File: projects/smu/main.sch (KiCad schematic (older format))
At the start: 4 parts, among them P101 CONN_01X15, P102 CONN_01X28, P103 CONN_01X15, P105 CONN_01X04

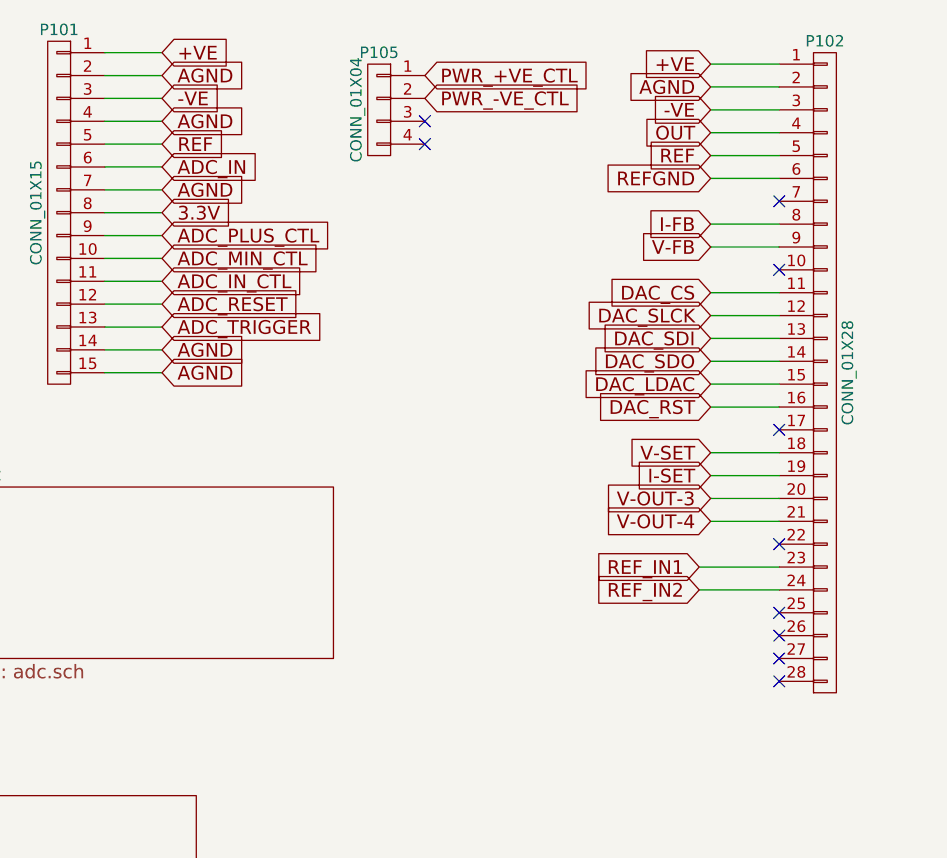
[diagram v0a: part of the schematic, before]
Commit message: add output section
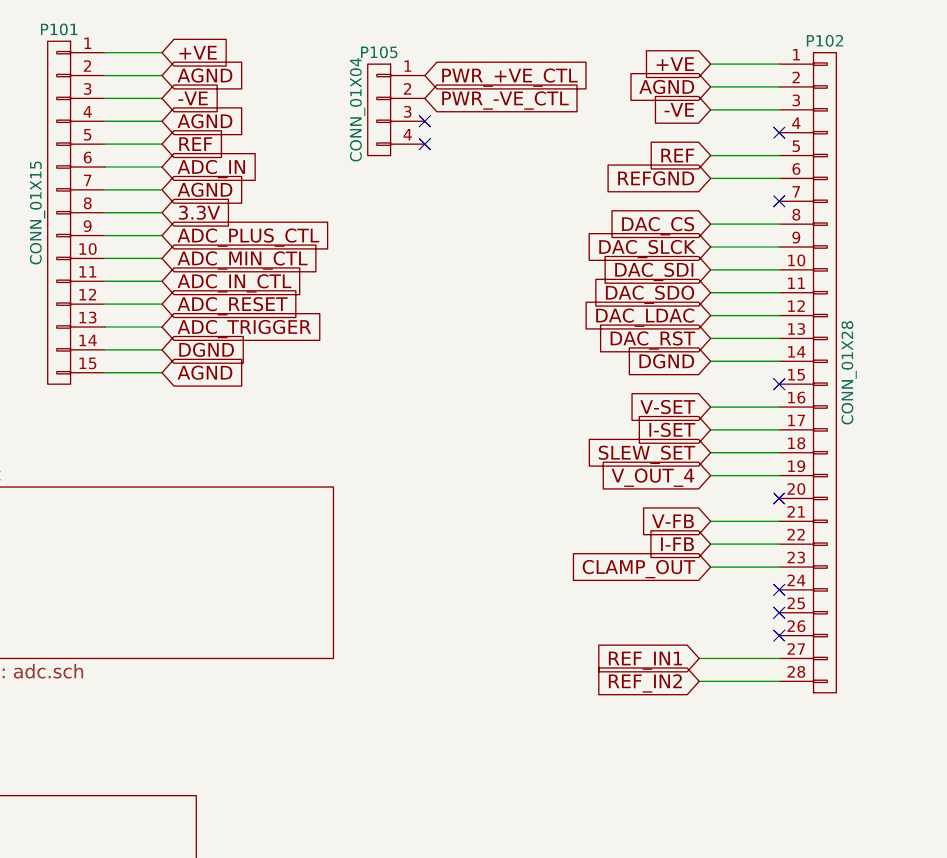
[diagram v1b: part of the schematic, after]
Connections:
- net V-OUT-4 is gone; now on net V-FB: P102.21 (P21)
- net AGND: now also P102.14 (P14)
- net DAC_CS: now also P102.8 (P8); no longer P102.11 (P11)
- net DAC_LDAC: now also P102.12 (P12); no longer P102.15 (P15)
- net DAC_RST: now also P102.13 (P13); no longer P102.16 (P16)
- net DAC_SDI: now also P102.10 (P10); no longer P102.13 (P13)
- net DAC_SDO: now also P102.11 (P11); no longer P102.14 (P14)
- net DAC_SLCK: now also P102.9 (P9); no longer P102.12 (P12)
- net I-FB: now also P102.22 (P22); no longer P102.8 (P8)
- net I-SET: now also P102.17 (P17); no longer P102.19 (P19)
- net REF_IN1: now also P102.27 (P27); no longer P102.23 (P23)
- net REF_IN2: now also P102.28 (P28); no longer P102.24 (P24)
- net V-FB: no longer P102.9 (P9)
- net V-SET: now also P102.16 (P16); no longer P102.18 (P18)
- net OUT: no longer names the net of P102.4 (P4)
- net V-OUT-3: no longer names the net of P102.20 (P20)
- new net CLAMP_OUT: P102.23 (P23)
- new net SLEW_SET: P102.18 (P18)
- new net V_OUT_4: P102.19 (P19)
- no-connect marks 22 -> 21
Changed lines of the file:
@@
 AGND
 Text GLabel 2400 2250 2    60   Input ~ 0
-AGND
+DGND
 Text GLabel 2400 2350 2    60   Input ~ 0
 AGND
 Text GLabel 2400 2150 2    60   Input ~ 0
 ADC_TRIGGER
-Wire Wire Line
-	2150 950  2400 950
-Wire Wire Line
-	2150 1050 2400 1050
-Wire Wire Line
-	2150 1150 2400 1150
-Wire Wire Line
-	2150 1350 2400 1350
-Wire Wire Line
-	2150 1450 2400 1450
-Wire Wire Line
-	2150 1650 2400 1650
-Wire Wire Line
-	2150 1750 2400 1750
-Wire Wire Line
-	2150 1850 2400 1850
-Wire Wire Line
-	2150 1250 2400 1250
-Wire Wire Line
-	2150 1550 2400 1550
-Wire Wire Line
-	2150 1950 2400 1950
-Wire Wire Line
-	2150 2050 2400 2050
-Wire Wire Line
-	2150 2150 2400 2150
-Wire Wire Line
-	2150 2250 2400 2250
-Wire Wire Line
-	2400 2350 2150 2350
-Wire Wire Line
-	5100 1000 4800 1000
-Wire Wire Line
-	5100 1100 4800 1100
-Wire Wire Line
-	5100 1200 4800 1200
-Wire Wire Line
-	5100 1300 4800 1300
-Wire Wire Line
-	4800 1400 5100 1400
-Wire Wire Line
-	5100 1800 4800 1800
-Wire Wire Line
-	4800 1700 5100 1700
 Text GLabel 7050 1500 3    60   Input ~ 0
 +VE
@@
 	1    0    0    -1
 $EndComp
-Wire Wire Line
-	7050 1300 7050 1500
 $Comp
 L PWR_FLAG #FLG02
@@
 Text GLabel 7650 1500 3    60   Input ~ 0
 -VE
-Wire Wire Line
-	7650 1300 7650 1500
-Wire Wire Line
-	4800 2000 5100 2000
-Wire Wire Line
-	4800 2100 5100 2100
-Wire Wire Line
-	4800 2200 5100 2200
-Wire Wire Line
-	4800 2300 5100 2300
-Wire Wire Line
-	4800 2400 5100 2400
-Wire Wire Line
-	4800 2500 5100 2500
 Text GLabel 9200 1400 0    60   Input ~ 0
 AGND
@@
 Text GLabel 9200 1600 0    60   Input ~ 0
 REFGND
-Wire Wire Line
-	9200 1400 9200 1600
-Wire Wire Line
-	4800 2700 5100 2700
-Wire Wire Line
-	4800 2800 5100 2800
-Wire Wire Line
-	4800 2900 5100 2900
-Wire Wire Line
-	4800 3000 5100 3000
-Wire Wire Line
-	4750 3200 5100 3200
-Wire Wire Line
-	4750 3300 5100 3300
-Wire Wire Line
-	4800 1500 5100 1500
 Text GLabel 4800 1000 0    60   Input ~ 0
 +VE
@@
 Text GLabel 4800 1400 0    60   Input ~ 0
 REF
+Text GLabel 4800 3100 0    60   Input ~ 0
+I-FB
+Text GLabel 4800 3200 0    60   Input ~ 0
+CLAMP_OUT
+Text GLabel 4800 3000 0    60   Input ~ 0
+V-FB
+Text GLabel 4800 2700 0    60   Input ~ 0
+SLEW_SET
+Text GLabel 4800 2800 0    60   Input ~ 0
+V_OUT_4
 Text GLabel 4800 1700 0    60   Input ~ 0
-I-FB
-Text GLabel 4800 1300 0    60   Input ~ 0
-OUT
-NoConn ~ 5100 1900
+DAC_CS
 Text GLabel 4800 1800 0    60   Input ~ 0
-V-FB
-Text GLabel 4800 2900 0    60   Input ~ 0
-V-OUT-3
-Text GLabel 4800 3000 0    60   Input ~ 0
-V-OUT-4
+DAC_SLCK
+Text GLabel 4800 1900 0    60   Input ~ 0
+DAC_SDI
 Text GLabel 4800 2000 0    60   Input ~ 0
-DAC_CS
+DAC_SDO
 Text GLabel 4800 2100 0    60   Input ~ 0
-DAC_SLCK
+DAC_LDAC
 Text GLabel 4800 2200 0    60   Input ~ 0
-DAC_SDI
-Text GLabel 4800 2300 0    60   Input ~ 0
-DAC_SDO
-Text GLabel 4800 2400 0    60   Input ~ 0
-DAC_LDAC
-Text GLabel 4800 2500 0    60   Input ~ 0
 DAC_RST
 Text GLabel 9200 1400 0    60   Input ~ 0
@@
 Text GLabel 9200 1600 0    60   Input ~ 0
 REFGND
-Text GLabel 4800 2700 0    60   Input ~ 0
+Text GLabel 4800 2500 0    60   Input ~ 0
 V-SET
-Text GLabel 4800 2800 0    60   Input ~ 0
+Text GLabel 4800 2600 0    60   Input ~ 0
 I-SET
 NoConn ~ 5100 1600
-NoConn ~ 5100 2600
-NoConn ~ 5100 3100
-NoConn ~ 5100 3600
-NoConn ~ 5100 3700
 Text GLabel 4800 1500 0    60   Input ~ 0
 REFGND
@@
 	1    0    0    -1
 $EndComp
-Text GLabel 4750 3300 0    60   Input ~ 0
+Text GLabel 4750 3700 0    60   Input ~ 0
 REF_IN2
-Text GLabel 4750 3200 0    60   Input ~ 0
+Text GLabel 4750 3600 0    60   Input ~ 0
 REF_IN1
 NoConn ~ 5100 3400
@@
 F1 "filter.sch" 60
 $EndSheet
+Wire Wire Line
+	2150 950  2400 950
+Wire Wire Line
+	2150 1050 2400 1050
+Wire Wire Line
+	2150 1150 2400 1150
+Wire Wire Line
+	2150 1350 2400 1350
+Wire Wire Line
+	2150 1450 2400 1450
+Wire Wire Line
+	2150 1650 2400 1650
+Wire Wire Line
+	2150 1750 2400 1750
+Wire Wire Line
+	2150 1850 2400 1850
+Wire Wire Line
+	2150 1250 2400 1250
+Wire Wire Line
+	2150 1550 2400 1550
+Wire Wire Line
+	2150 1950 2400 1950
+Wire Wire Line
+	2150 2050 2400 2050
+Wire Wire Line
+	2150 2150 2400 2150
+Wire Wire Line
+	2150 2250 2400 2250
+Wire Wire Line
+	2400 2350 2150 2350
+Wire Wire Line
+	5100 1000 4800 1000
+Wire Wire Line
+	5100 1100 4800 1100
+Wire Wire Line
+	5100 1200 4800 1200
+Wire Wire Line
+	4800 1400 5100 1400
+Wire Wire Line
+	7050 1300 7050 1500
+Wire Wire Line
+	7650 1300 7650 1500
+Wire Wire Line
+	9200 1400 9200 1600
+Wire Wire Line
+	4800 1500 5100 1500
+Wire Wire Line
+	4800 1700 5100 1700
+Wire Wire Line
+	4800 1800 5100 1800
+Wire Wire Line
+	4800 1900 5100 1900
+Wire Wire Line
+	4800 2000 5100 2000
+Wire Wire Line
+	4800 2100 5100 2100
+Wire Wire Line
+	4800 2200 5100 2200
+Text GLabel 4800 2300 0    60   Input ~ 0
+DGND
+Wire Wire Line
+	4800 2300 5100 2300
+Wire Wire Line
+	4800 2500 5100 2500
+Wire Wire Line
+	4800 2600 5100 2600
+Wire Wire Line
+	4800 2700 5100 2700
+Wire Wire Line
+	4800 2800 5100 2800
+NoConn ~ 5100 2400
+NoConn ~ 5100 2900
+Wire Wire Line
+	4800 3000 5100 3000
+Wire Wire Line
+	4800 3100 5100 3100
+Wire Wire Line
+	4800 3200 5100 3200
+NoConn ~ 5100 3300
+Wire Wire Line
+	4750 3600 5100 3600
+Wire Wire Line
+	4750 3700 5100 3700
+NoConn ~ 5100 1300
 $EndSCHEMATC

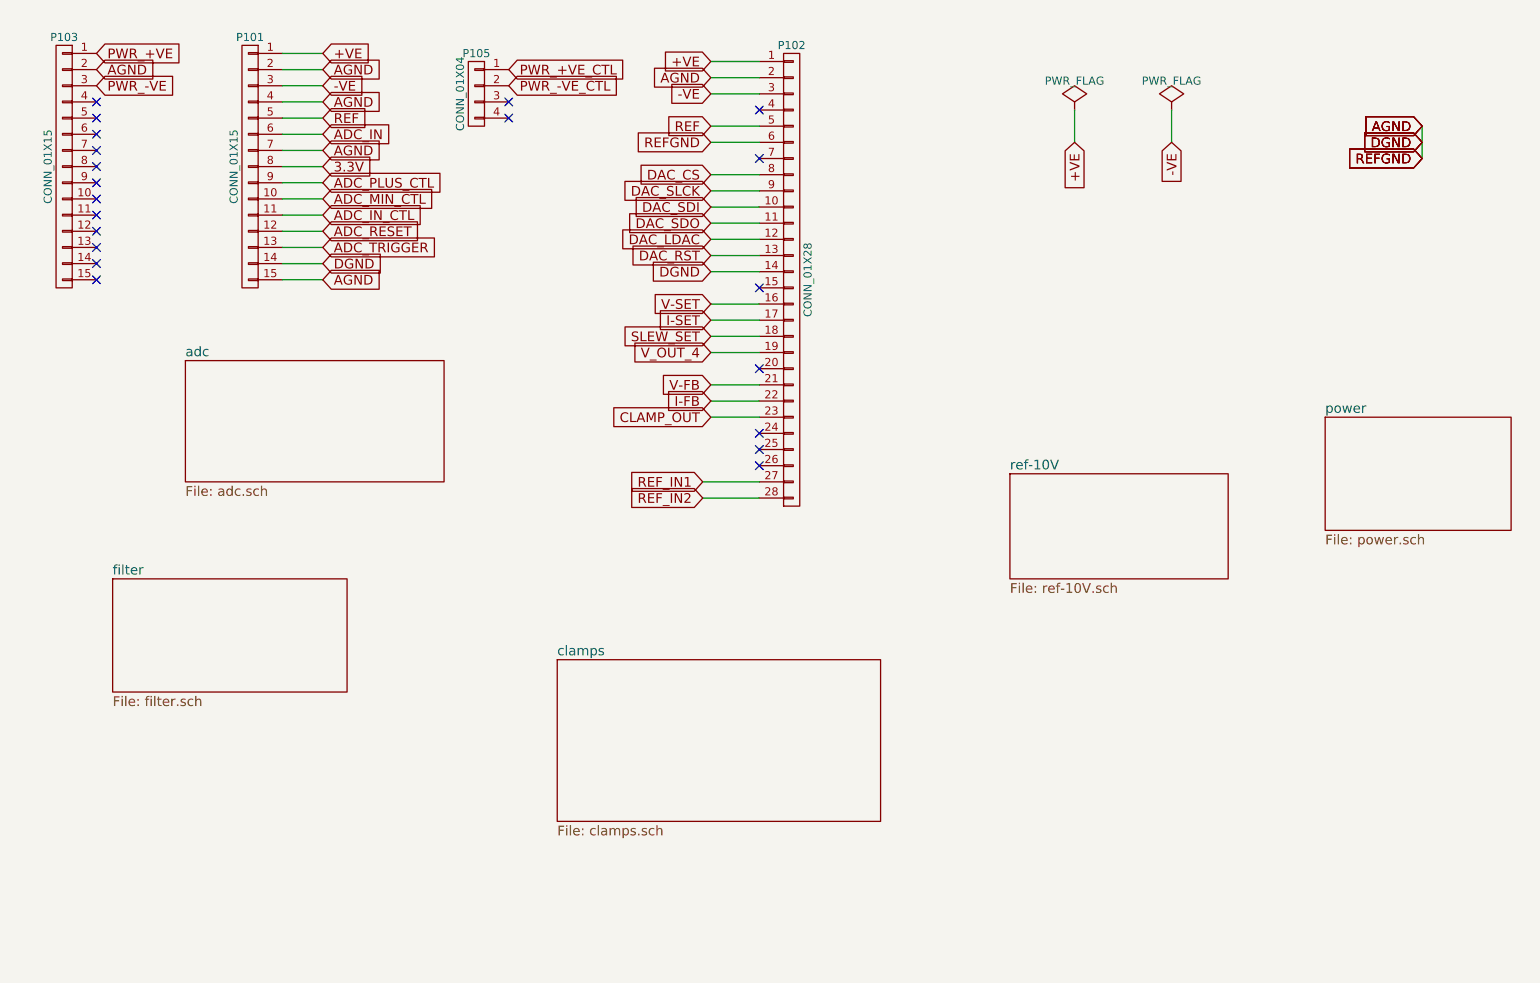
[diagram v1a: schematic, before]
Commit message: split pin-headers into analog and digital
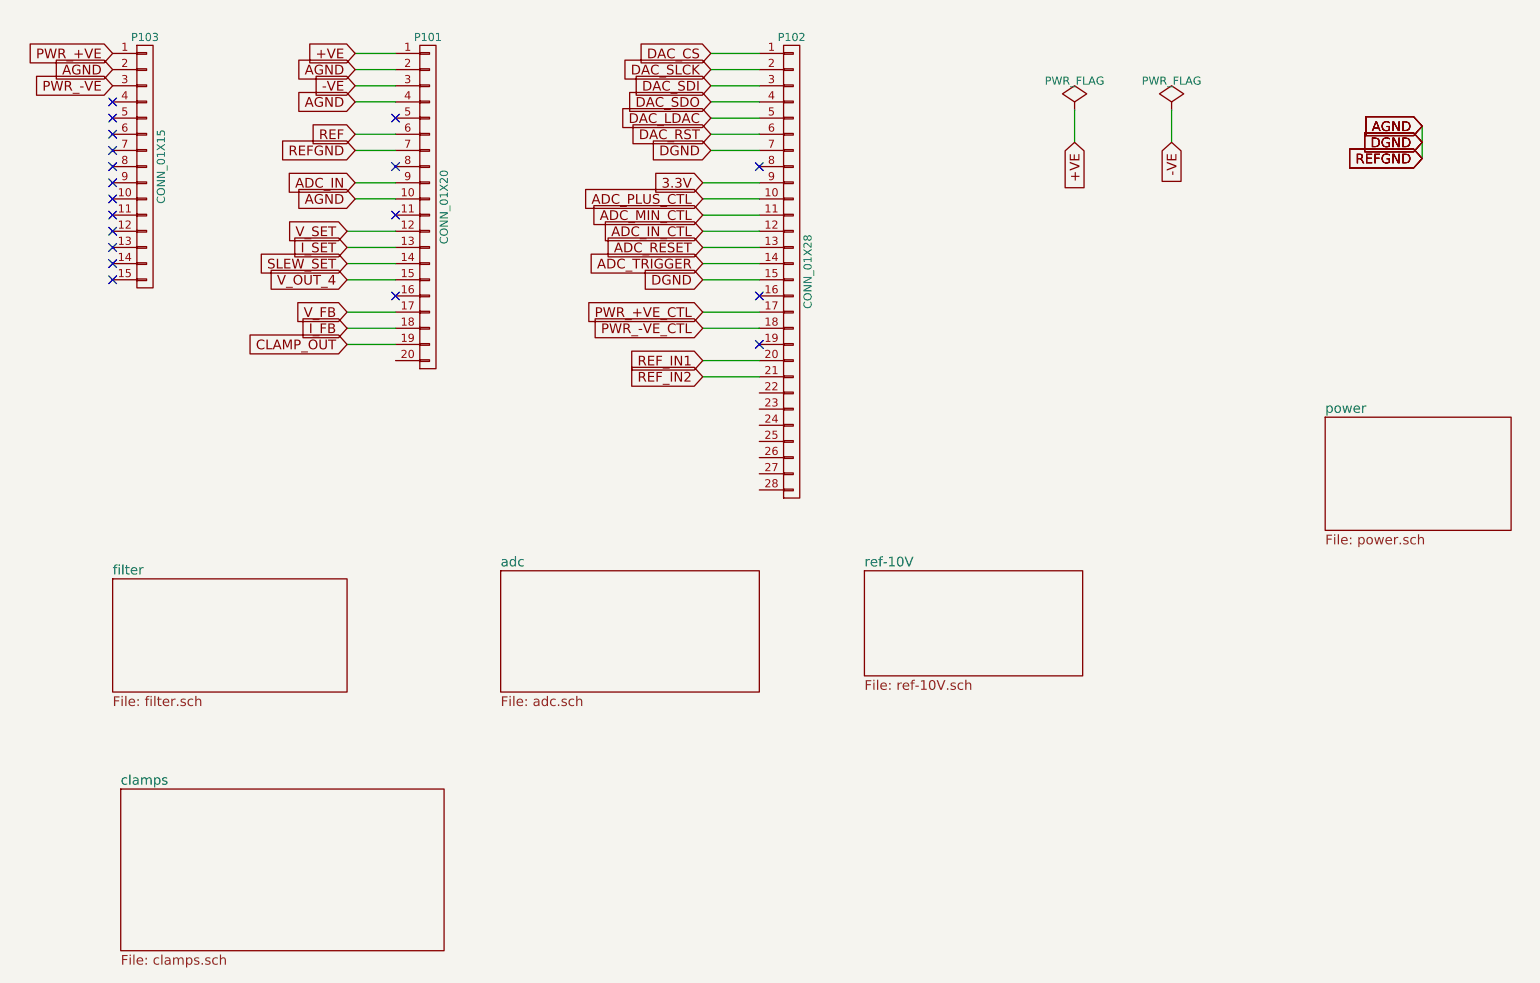
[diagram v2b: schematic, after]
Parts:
- removed P101: CONN_01X15, Pin_Headers:Pin_Header_Straight_1x15, symbol CONN_01X15
- removed P105: CONN_01X04, symbol CONN_01X04
- added P101: CONN_01X20, symbol CONN_01X20
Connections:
- net I-SET is gone; now on net PWR_+VE_CTL: P102.17 (P17)
- net V-FB is gone; now on net REF_IN2: P102.21 (P21)
- net +VE: now also P101.1 (P1); no longer P102.1 (P1)
- net -VE: now also P101.3 (P3); no longer P102.3 (P3)
- net 3.3V: now also P102.9 (P9)
- net ADC_IN: now also P101.9 (P9)
- net ADC_IN_CTL: now also P102.12 (P12)
- net ADC_MIN_CTL: now also P102.11 (P11)
- net ADC_PLUS_CTL: now also P102.10 (P10)
- net ADC_RESET: now also P102.13 (P13)
- net ADC_TRIGGER: now also P102.14 (P14)
- net AGND: now also P102.15 (P15), P102.7 (P7), P101.10 (P10), P101.2 (P2), P101.4 (P4), P101.7 (P7); no longer P102.14 (P14), P102.2 (P2), P102.6 (P6)
- net CLAMP_OUT: now also P101.19 (P19); no longer P102.23 (P23)
- net DAC_CS: now also P102.1 (P1); no longer P102.8 (P8)
- net DAC_LDAC: now also P102.5 (P5); no longer P102.12 (P12)
- net DAC_RST: now also P102.6 (P6); no longer P102.13 (P13)
- net DAC_SDI: now also P102.3 (P3); no longer P102.10 (P10)
- net DAC_SDO: now also P102.4 (P4); no longer P102.11 (P11)
- net DAC_SLCK: now also P102.2 (P2); no longer P102.9 (P9)
- net PWR_-VE_CTL: now also P102.18 (P18)
- net REF: now also P101.6 (P6); no longer P102.5 (P5)
- net REF_IN1: now also P102.20 (P20); no longer P102.27 (P27)
- net REF_IN2: no longer P102.28 (P28)
- net SLEW_SET: now also P101.14 (P14); no longer P102.18 (P18)
- net V_OUT_4: now also P101.15 (P15); no longer P102.19 (P19)
- net I-FB: no longer names the net of P102.22 (P22)
- net V-SET: no longer names the net of P102.16 (P16)
- new net I_FB: P101.18 (P18)
- new net I_SET: P101.13 (P13)
- new net V_FB: P101.17 (P17)
- new net V_SET: P101.12 (P12)
- no-connect marks 21 -> 19
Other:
- moved on the sheet: P102, P103
